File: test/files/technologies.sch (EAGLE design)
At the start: 16 parts

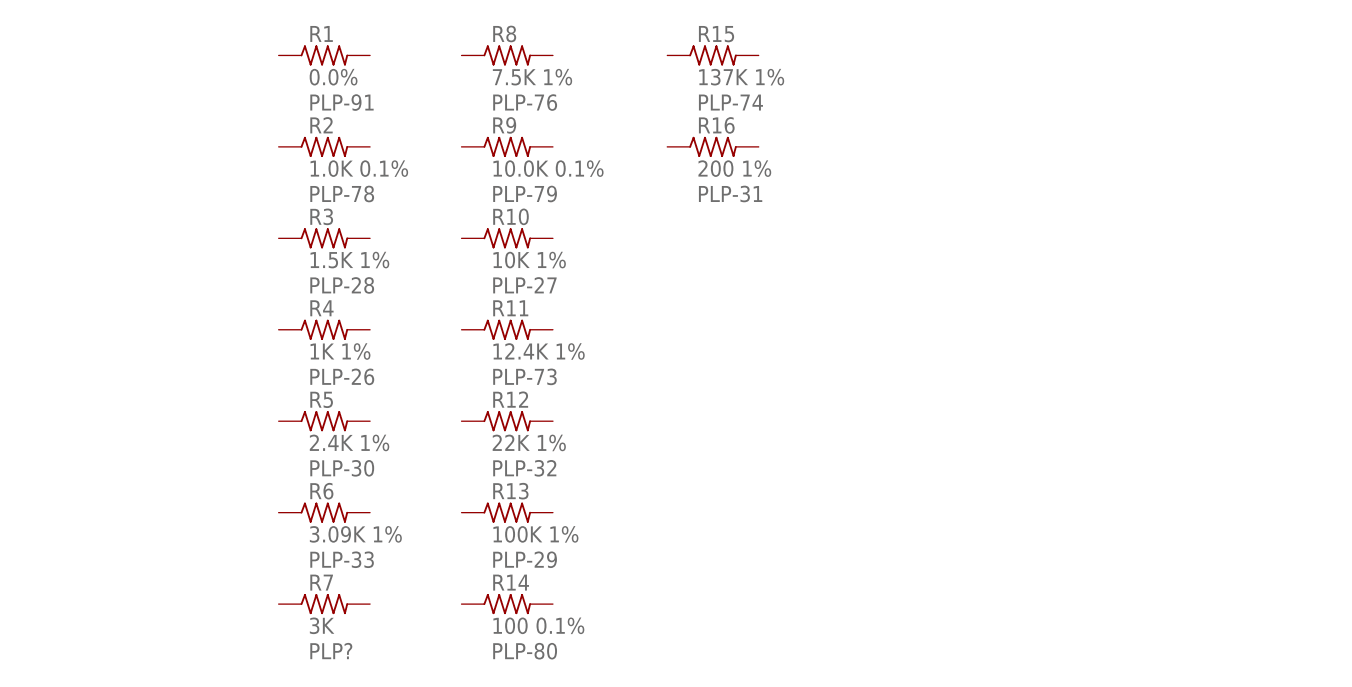
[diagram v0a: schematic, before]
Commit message: Added several variants to technologies.sch
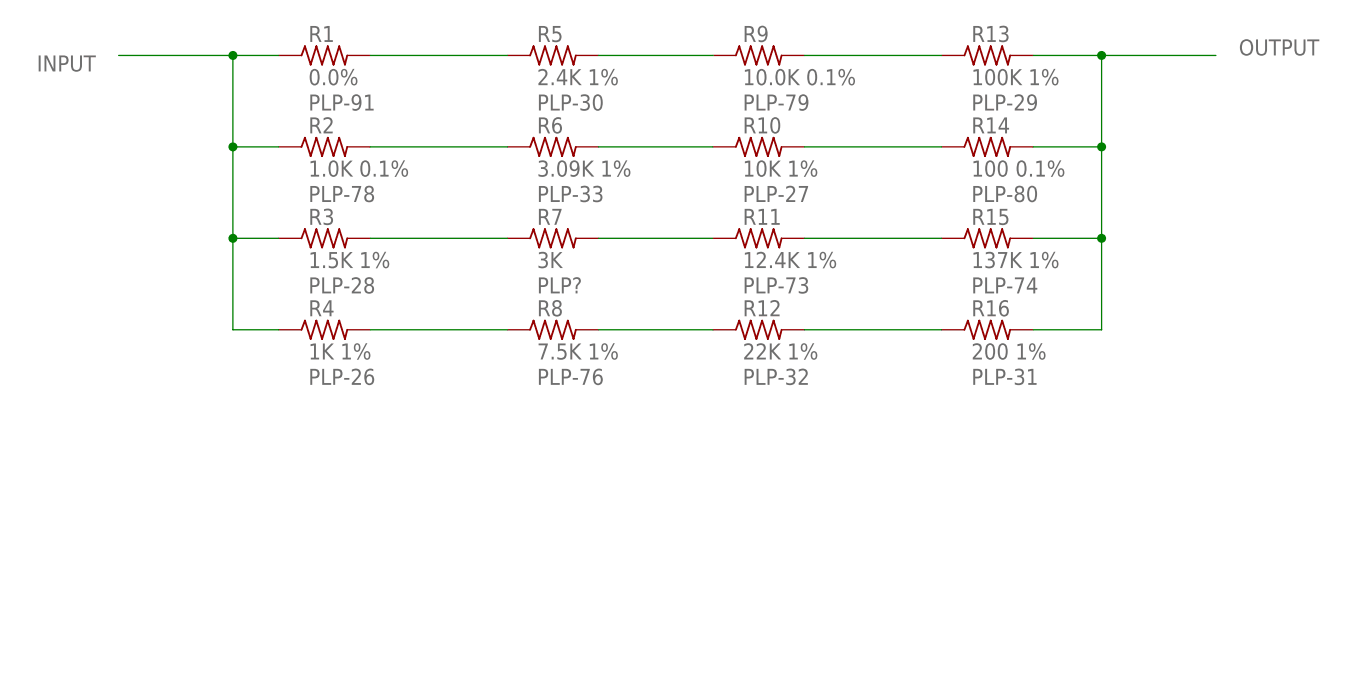
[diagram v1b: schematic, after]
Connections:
- new net INPUT: R1.1, R2.1, R3.1, R4.1
- new net N$10: R13.1, R9.2
- new net N$12: R10.2, R14.1
- new net N$13: R11.2, R15.1
- new net N$14: R12.2, R16.1
- new net N$2: R1.2, R5.1
- new net N$3: R2.2, R6.1
- new net N$4: R3.2, R7.1
- new net N$5: R4.2, R8.1
- new net N$6: R12.1, R8.2
- new net N$7: R11.1, R7.2
- new net N$8: R10.1, R6.2
- new net N$9: R5.2, R9.1
- new net OUTPUT: R13.2, R14.2, R15.2, R16.2
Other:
- moved on the sheet: R10, R11, R12, R13, R14, R15, R16, R5, R6, R7, R8, R9
